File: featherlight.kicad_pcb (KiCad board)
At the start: 4 copper layers, 88.9 x 88.9 mm, 97 parts, among them IC1 BNO055, P1 USB_OTG, P10 CONN_01X06, P11 CONN_01X06, P12 CONN_01X06, P13 CONN_01X06, P14 CONN_01X06, P15 CONN_01X06, P16 CONN_01X06, P17 CONN_01X01, P18 CONN_01X01, P19 CONN_01X02, P2 CONN_01X06, P3 CONN_01X06, P4 CONN_01X06, P5 CONN_01X06, P6 CONN_01X06, P7 CONN_01X06, P8 CONN_01X06, P9 CONN_01X06, SW1 Button, SW2 Button, SW3 Button, SW4 Button, SW5 Button, U1 74AHCT1G125, U2 SAMD21G18, U3 AP2112, U4 MCP73831, Y1 32.768 KHz, Y2 32.768 KHz

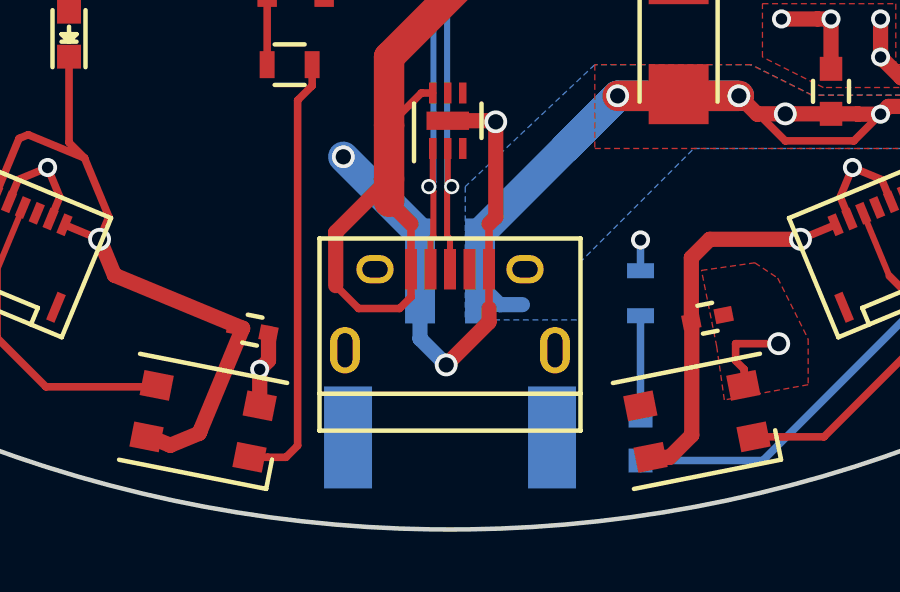
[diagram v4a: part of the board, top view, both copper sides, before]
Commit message: Changed PTH on the USB footprint to circular drills since Oshpark cannot into slots.
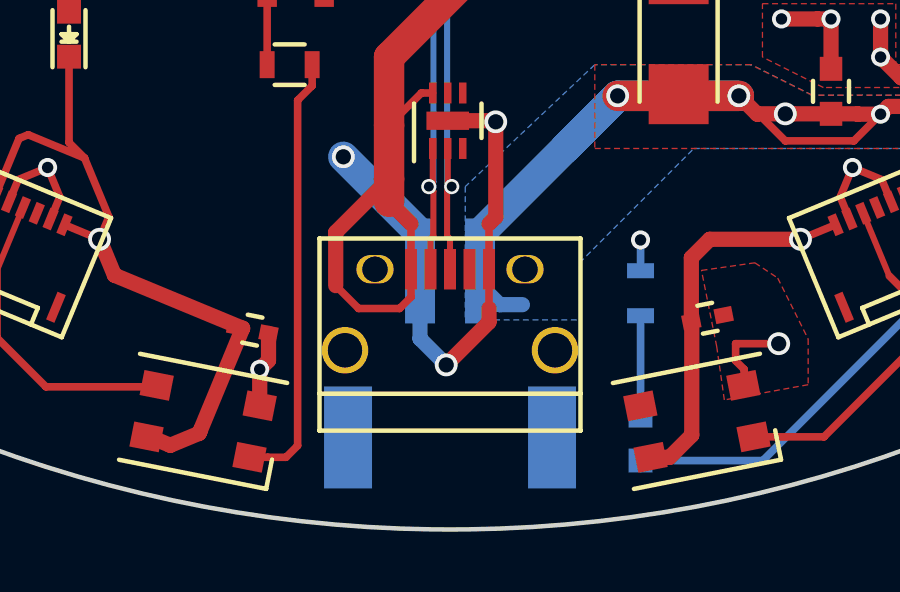
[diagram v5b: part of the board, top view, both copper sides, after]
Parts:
- P1: footprint Connect:USB_Micro-B -> featherlight:USB_Micro-B
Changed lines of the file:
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@@
-(kicad_pcb (version 20160815) (host pcbnew 4.1.0-alpha+201609050731+7118~50~ubuntu16.04.1-product)
+(kicad_pcb (version 20160815) (host pcbnew 4.1.0-alpha+201609080933+7135~55~ubuntu16.04.1-product)
   (general
     (links 297)
     (no_connects 3)
-    (area 57.074999 57.074999 146.125001 146.125001)
+    (area 54.872313 54.953833 148.378573 148.330281)
     (thickness 1.6002)
     (drawings 4)
@@
   )
   (setup
-    (last_trace_width 0.254)
+    (last_trace_width 0.2032)
     (user_trace_width 0.1524)
     (user_trace_width 0.2032)
@@
     )
   )
-  (module Connect:USB_Micro-B (layer F.Cu)
-    (at 101.6 138.938)
-    (descr "Micro USB Type B Receptacle")
-    (tags "USB USB_B USB_micro USB_OTG")
-    (attr smd)
-    (fp_text reference P1 (at 0 -3.45) (layer F.SilkS) hide
-      (effects (font (size 1 1) (thickness 0.15)))
-    )
-    (fp_text value USB_OTG (at 0 4.8) (layer F.Fab)
-      (effects (font (size 1 1) (thickness 0.15)))
-    )
-    (fp_line (start -4.6 -2.8) (end 4.6 -2.8) (layer F.CrtYd) (width 0.05))
-    (fp_line (start 4.6 -2.8) (end 4.6 4.05) (layer F.CrtYd) (width 0.05))
-    (fp_line (start 4.6 4.05) (end -4.6 4.05) (layer F.CrtYd) (width 0.05))
-    (fp_line (start -4.6 4.05) (end -4.6 -2.8) (layer F.CrtYd) (width 0.05))
-    (fp_line (start -4.3509 3.81746) (end 4.3491 3.81746) (layer F.SilkS) (width 0.15))
-    (fp_line (start -4.3509 -2.58754) (end 4.3491 -2.58754) (layer F.SilkS) (width 0.15))
-    (fp_line (start 4.3491 -2.58754) (end 4.3491 3.81746) (layer F.SilkS) (width 0.15))
-    (fp_line (start 4.3491 2.58746) (end -4.3509 2.58746) (layer F.SilkS) (width 0.15))
-    (fp_line (start -4.3509 3.81746) (end -4.3509 -2.58754) (layer F.SilkS) (width 0.15))
-    (pad 1 smd rect (at -1.3009 -1.56254 90) (size 1.35 0.4) (layers F.Cu F.Paste F.Mask)
-      (net 42 VUSB))
-    (pad 2 smd rect (at -0.6509 -1.56254 90) (size 1.35 0.4) (layers F.Cu F.Paste F.Mask)
-      (net 20 D-))
-    (pad 3 smd rect (at -0.0009 -1.56254 90) (size 1.35 0.4) (layers F.Cu F.Paste F.Mask)
-      (net 21 D+))
-    (pad 4 smd rect (at 0.6491 -1.56254 90) (size 1.35 0.4) (layers F.Cu F.Paste F.Mask))
-    (pad 5 smd rect (at 1.2991 -1.56254 90) (size 1.35 0.4) (layers F.Cu F.Paste F.Mask)
-      (net 1 GND))
-    (pad 6 thru_hole oval (at -2.5009 -1.56254 90) (size 0.95 1.25) (drill oval 0.55 0.85) (layers *.Cu *.Mask F.SilkS)
-      (net 28 "Net-(P1-Pad6)"))
-    (pad 6 thru_hole oval (at 2.4991 -1.56254 90) (size 0.95 1.25) (drill oval 0.55 0.85) (layers *.Cu *.Mask F.SilkS)
-      (net 28 "Net-(P1-Pad6)"))
-    (pad 6 thru_hole oval (at -3.5009 1.13746 90) (size 1.55 1) (drill oval 1.15 0.5) (layers *.Cu *.Mask F.SilkS)
-      (net 28 "Net-(P1-Pad6)"))
-    (pad 6 thru_hole oval (at 3.4991 1.13746 90) (size 1.55 1) (drill oval 1.15 0.5) (layers *.Cu *.Mask F.SilkS)
-      (net 28 "Net-(P1-Pad6)"))
-  )
   (module "Connector-FFC:Molex 503480-600" (layer F.Cu)
     (at 87.019761 136.79981 337.5)
@@
     )
   )
+  (module featherlight:USB_Micro-B (layer F.Cu)
+    (at 101.6 138.938)
+    (descr "Micro USB Type B Receptacle with circular plated through holes")
+    (tags "USB USB_B USB_micro USB_OTG")
+    (attr smd)
+    (fp_text reference P1 (at 0 -3.45) (layer F.SilkS) hide
+      (effects (font (size 1 1) (thickness 0.15)))
+    )
+    (fp_text value USB_OTG (at 0 4.8) (layer F.Fab)
+      (effects (font (size 1 1) (thickness 0.15)))
+    )
+    (fp_line (start -4.6 -2.8) (end 4.6 -2.8) (layer F.CrtYd) (width 0.05))
+    (fp_line (start 4.6 -2.8) (end 4.6 4.05) (layer F.CrtYd) (width 0.05))
+    (fp_line (start 4.6 4.05) (end -4.6 4.05) (layer F.CrtYd) (width 0.05))
+    (fp_line (start -4.6 4.05) (end -4.6 -2.8) (layer F.CrtYd) (width 0.05))
+    (fp_line (start -4.3509 3.81746) (end 4.3491 3.81746) (layer F.SilkS) (width 0.15))
+    (fp_line (start -4.3509 -2.58754) (end 4.3491 -2.58754) (layer F.SilkS) (width 0.15))
+    (fp_line (start 4.3491 -2.58754) (end 4.3491 3.81746) (layer F.SilkS) (width 0.15))
+    (fp_line (start 4.3491 2.58746) (end -4.3509 2.58746) (layer F.SilkS) (width 0.15))
+    (fp_line (start -4.3509 3.81746) (end -4.3509 -2.58754) (layer F.SilkS) (width 0.15))
+    (pad 1 smd rect (at -1.3009 -1.56254 90) (size 1.35 0.4) (layers F.Cu F.Paste F.Mask)
+      (net 42 VUSB))
+    (pad 2 smd rect (at -0.6509 -1.56254 90) (size 1.35 0.4) (layers F.Cu F.Paste F.Mask)
+      (net 20 D-))
+    (pad 3 smd rect (at -0.0009 -1.56254 90) (size 1.35 0.4) (layers F.Cu F.Paste F.Mask)
+      (net 21 D+))
+    (pad 4 smd rect (at 0.6491 -1.56254 90) (size 1.35 0.4) (layers F.Cu F.Paste F.Mask))
+    (pad 5 smd rect (at 1.2991 -1.56254 90) (size 1.35 0.4) (layers F.Cu F.Paste F.Mask)
+      (net 1 GND))
+    (pad 6 thru_hole oval (at -2.5009 -1.56254 90) (size 0.95 1.25) (drill 0.85) (layers *.Cu *.Mask F.SilkS)
+      (net 28 "Net-(P1-Pad6)"))
+    (pad 6 thru_hole oval (at 2.4991 -1.56254 90) (size 0.95 1.25) (drill 0.85) (layers *.Cu *.Mask F.SilkS)
+      (net 28 "Net-(P1-Pad6)"))
+    (pad 6 thru_hole circle (at -3.5009 1.13746 90) (size 1.55 1.55) (drill 1.15) (layers *.Cu *.Mask F.SilkS)
+      (net 28 "Net-(P1-Pad6)"))
+    (pad 6 thru_hole circle (at 3.4991 1.13746 90) (size 1.55 1.55) (drill 1.15) (layers *.Cu *.Mask F.SilkS)
+      (net 28 "Net-(P1-Pad6)"))
+  )
   (gr_text SWCLK (at 116.84 112.776) (layer B.SilkS)

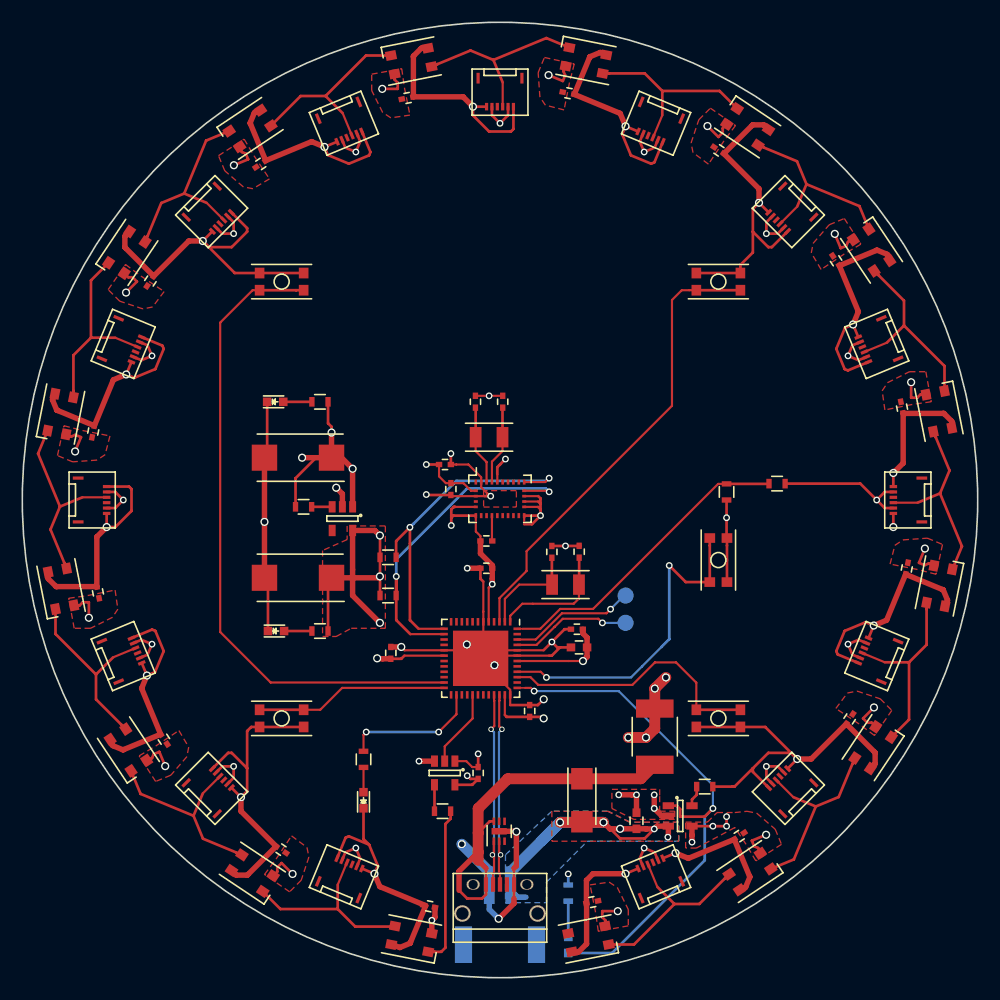
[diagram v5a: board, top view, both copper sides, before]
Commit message: Improper board size required full PCB redesign.
The rev A PCBs were far bigger than intended (target diameter was used as radius when laying it out).

Removed lipo circuit while reworking layout; will try to add it back in later.
Moved USB port to very edge of board to permit cable access.
Added +5V and ground contacts to ISP pads.
Swapped down to SAMD21E MCU for space reasons.
Removed connectors for space reasons.  Maybe they'll fit on the bottom?
Added fiducials front and back.
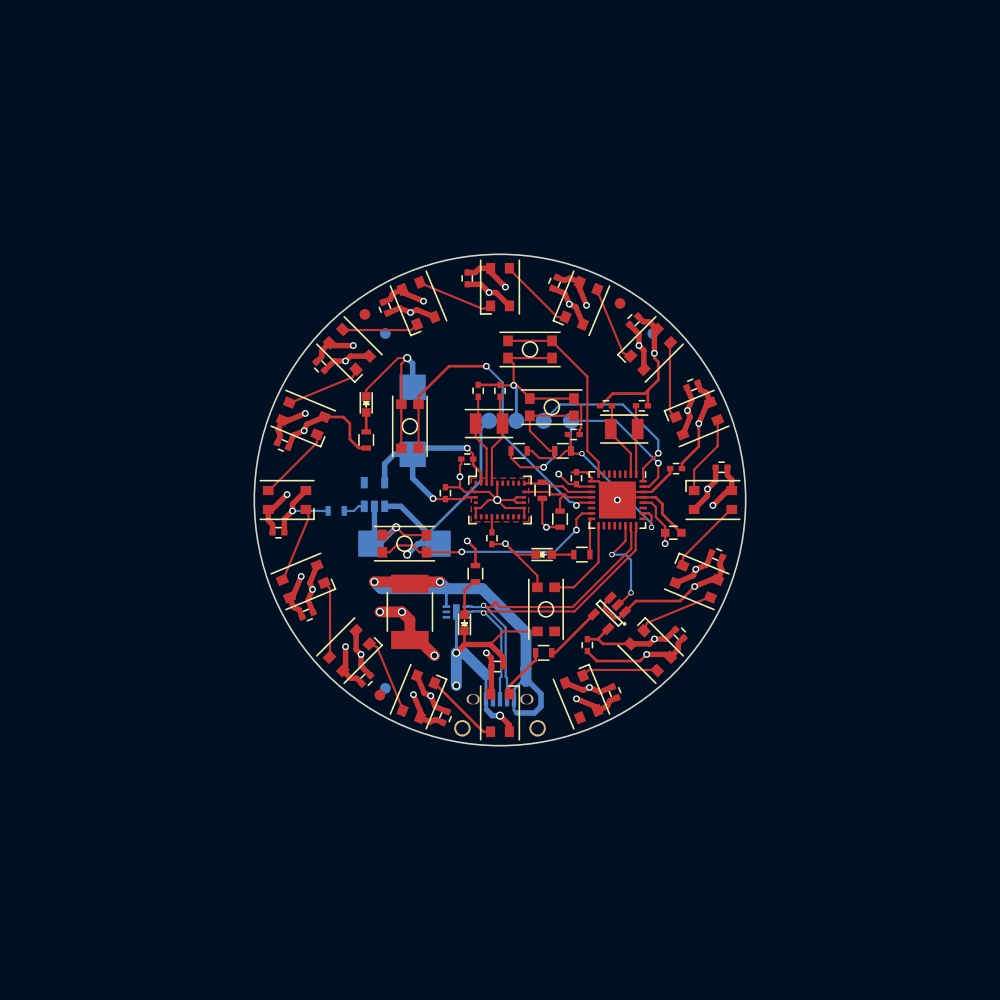
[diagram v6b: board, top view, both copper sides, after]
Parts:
- removed C20: 0.1 uF, Capacitors_SMD:C_0402
- removed C32: 4.7 uF, Capacitors_SMD:C_0603
- removed D21: D_Schottky, featherlight:DO-214AC
- removed D22: Green, LEDs:LED_0603
- removed P10, P11, P12, P13, P14, P15, P16, P2, P7, P8, P9: CONN_01X06, Connector-FFC:Molex 503480-600
- removed P17, P18: CONN_01X01, Measurement_Points:Measurement_Point_Round-SMD-Pad_Small
- removed P19: CONN_01X02, Connectors_JST:JST_PH_S2B-PH-SM4-TB_02x2.00mm_Angled
- removed R10: 10 K, Resistors_SMD:R_0603
- removed R11: 100 K, Resistors_SMD:R_0603
- removed U4: MCP73831, TO_SOT_Packages_SMD:SOT-23-5
- added FID1: Fiducial, Fiducials:Fiducial_1mm_Dia_2.54mm_Outer_CopperTop, F.Cu at (89.0, 84.3)
- added FID2: Fiducial, Fiducials:Fiducial_1mm_Dia_2.54mm_Outer_CopperTop, F.Cu at (112.8, 83.3)
- added FID3: Fiducial, Fiducials:Fiducial_1mm_Dia_2.54mm_Outer_CopperTop, F.Cu at (90.4, 119.8)
- added FID4: Fiducial, Fiducials:Fiducial_1mm_Dia_2.54mm_Outer_CopperTop, B.Cu at (90.9, 86.1)
- added FID5: Fiducial, Fiducials:Fiducial_1mm_Dia_2.54mm_Outer_CopperTop, B.Cu at (90.9, 119.1)
- added FID6: Fiducial, Fiducials:Fiducial_1mm_Dia_2.54mm_Outer_CopperTop, B.Cu at (115.8, 86.1)
- added R12: 1 K, Resistors_SMD:R_0603, B.Cu at (107.4, 97.0)
- C17, C18, D17, P1, R2, U3: moved to B.Cu
- P3, P4, P5, P6: value CONN_01X06 -> CONN_01X01; footprint Connector-FFC:Molex 503480-600 -> Measurement_Points:Measurement_Point_Round-SMD-Pad_Small; moved to B.Cu
- R5: value 100 K -> 10 K
- R9: moved to F.Cu
- U2: value SAMD21G18 -> SAMD21E18A-M; footprint Housings_DFN_QFN:QFN-48-1EP_7x7mm_Pitch0.5mm -> Housings_DFN_QFN:QFN-32-1EP_5x5mm_Pitch0.5mm
- moved P3 48.0 mm to (108.2, 94.2), turned to 0 degrees
- moved P4 45.0 mm to (105.7, 94.2), turned to 0 degrees
- moved R9 41.2 mm to (107.4, 97.0), turned to 180 degrees
- moved P5 37.8 mm to (100.6, 94.2), turned to 0 degrees
- moved P6 37.4 mm to (103.1, 94.2), turned to 0 degrees
- moved D18 28.3 mm to (105.7, 106.7), turned to 0 degrees
- moved R6 27.9 mm to (109.2, 106.7), turned to 0 degrees
- moved C19 26.5 mm to (108.5, 95.5), turned to 180 degrees
- moved F1 25.6 mm to (93.2, 112.0), turned to 270 degrees
- moved R5 24.2 mm to (103.4, 97.0)
- moved C1 23.2 mm to (101.3, 117.1), turned to 0 degrees
- moved D1 22.6 mm to (101.6, 121.4), turned to 90 degrees
- moved D16 22.6 mm to (109.2, 119.9), turned to 112.5 degrees
- moved D10 22.5 mm to (109.2, 83.3), turned to 247.5 degrees
- moved D14 22.5 mm to (119.9, 109.2), turned to 157.5 degrees
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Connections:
- C19 pad 1: +3V3 -> GND
- C19 pad 2: GND -> /MCU + IMU/~RST~
- P3 pad 1: GND -> SWCLK
- P4 pad 1: GND -> SWDIO
- P5 pad 1: GND -> VDD
- R5 pad 1: VDD_MON -> +3V3
- R5 pad 2: VDD -> /MCU + IMU/~RST~
- R9 pad 1: VDD -> /MCU + IMU/~RST~
- R9 pad 2: Net-(D22-Pad2) -> Net-(R9-Pad2)
- SW1 pad 2: /MCU + IMU/~RST~ -> Net-(R9-Pad2)
- U2 pad 10: (no net) -> GND
- U2 pad 11: (no net) -> /MCU + IMU/SDA
- U2 pad 12: (no net) -> /MCU + IMU/SCL
- U2 pad 13: /MCU + IMU/SDA -> /MCU + IMU/UL_BUTTON
- U2 pad 14: /MCU + IMU/SCL -> (no net)
- U2 pad 15: (no net) -> /MCU + IMU/LL_BUTTON
- U2 pad 16: (no net) -> Net-(R6-Pad2)
- U2 pad 17: +3V3 -> /MCU + IMU/LR_BUTTON
- U2 pad 18: GND -> (no net)
- U2 pad 22: (no net) -> Net-(U1-Pad2)
- U2 pad 23: /MCU + IMU/UL_BUTTON -> D-
- U2 pad 24: /MCU + IMU/LL_BUTTON -> D+
- U2 pad 26: Net-(R6-Pad2) -> /MCU + IMU/~RST~
- U2 pad 28: (no net) -> GND
- U2 pad 29: Net-(U1-Pad2) -> +3V3
- U2 pad 3: /MCU + IMU/UR_BUTTON -> (no net)
- U2 pad 30: (no net) -> +3V3
- U2 pad 31: (no net) -> SWCLK
- U2 pad 32: (no net) -> SWDIO
- U2 pad 33: D- -> +3V3
- U2 pad 5: GND -> (no net)
- U2 pad 6: +3V3 -> (no net)
- U2 pad 8: (no net) -> /MCU + IMU/UR_BUTTON
- U2 pad 9: (no net) -> +3V3
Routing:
- net GND: track 470.2 -> 223.0 mm, vias 39 -> 26
- net CHARGE_STATUS: track 50.8 -> 0.00 mm, vias 2 -> 0
- net +3V3: track 106.6 -> 61.9 mm, vias 12 -> 6
- net +BATT: track 33.7 -> 0.00 mm, vias 5 -> 0
- net /MCU + IMU/UL_BUTTON: track 60.6 -> 30.4 mm, vias 0 -> 2
- net VDD_MON: track 29.0 -> 0.00 mm
- net VDD: track 150.7 -> 123.3 mm, vias 44 -> 20
- net /MCU + IMU/SDA: track 33.0 -> 6.61 mm, vias 2 -> 0
- net /MCU + IMU/UR_BUTTON: track 43.3 -> 18.3 mm
- net /MCU + IMU/SCL: track 31.9 -> 8.20 mm, vias 2 -> 0
- net SWDIO: track 0.00 -> 17.1 mm, vias 0 -> 1
- net /MCU + IMU/LR_BUTTON: track 25.2 -> 8.46 mm
- net SWCLK: track 0.00 -> 15.6 mm, vias 0 -> 1
- net /MCU + IMU/~RST~: track 31.2 -> 18.9 mm
- net /MCU + IMU/SWDIO: track 11.8 -> 0.00 mm, vias 1 -> 0
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- removed copper zone on F.Cu, net +3V3
- removed copper zone on B.Cu, net +BATT
- removed copper zone on F.Cu, net +BATT
- removed copper zone on F.Cu, net VDD
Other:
- board size 88.9 x 88.9 mm -> 45.7 x 45.7 mm
- net class Default: clearance 0.2032 -> 0.127
- net class Power: clearance 0.2032 -> 0.127
- rule trace_clearance: 0.2032 -> 0.127
- rule trace_min: 0.1524 -> 0.127
- rule via_min_drill: 0.3302 -> 0.254
- rule via_min_size: 0.508 -> 0.3556
- board text added: "+5"
- board text added: "Featherlight Rev B"
- board text added: "GND"
- board text removed: "Featherlight Prototype Rev B"

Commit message: Re-added lipo circuit.
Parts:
- added C20: 4.7 uF, Capacitors_SMD:C_0603, B.Cu at (106.4, 107.7)
- added D21: Green, LEDs:LED_0603, F.Cu at (106.4, 121.2)
- added D22: D_Schottky, featherlight:DO-214AC, F.Cu at (91.7, 100.8)
- added P2: CONN_01X02, Connectors_JST:JST_PH_S2B-PH-SM4-TB_02x2.00mm_Angled, B.Cu at (114.3, 114.0)
- added R10: 100 K, Resistors_SMD:R_0603, B.Cu at (111.0, 88.2)
- added R11: 470, Resistors_SMD:R_0603, B.Cu at (109.7, 121.4)
- added R13: 100 K, Resistors_SMD:R_0603, F.Cu at (111.0, 88.2)
- added R14: 10 K, Resistors_SMD:R_0603, B.Cu at (102.9, 108.7)
- added U4: MCP73831, TO_SOT_Packages_SMD:SOT-23-5, B.Cu at (105.9, 110.7)
- moved C24 0.78 mm to (112.0, 92.3), turned to 270 degrees
- renumbered D20 to D19, D19 to D20, R7 to R2, R8 to R7, R2 to R8
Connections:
- U2 pad 19: (no net) -> CHARGE_STATUS
- U2 pad 6: (no net) -> VDD_MON
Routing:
- net +BATT: track 0.00 -> 30.0 mm, vias 0 -> 2
- net CHARGE_STATUS: track 0.00 -> 28.5 mm, vias 0 -> 2
- net GND: track 223.0 -> 243.3 mm, vias 26 -> 27
- net VDD: track 123.3 -> 139.3 mm
- net VDD_MON: track 0.00 -> 12.2 mm, vias 0 -> 1
- net VUSB: track 38.7 -> 50.7 mm
- net Net-(R14-Pad1): track 0.00 -> 4.42 mm
- net Net-(D21-Pad2): track 0.00 -> 3.64 mm, vias 0 -> 1
- net /MCU + IMU/LL_BUTTON: track 22.1 -> 22.8 mm
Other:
- net class Default: clearance 0.127 -> 0.2032
- net class Power: clearance 0.127 -> 0.2032
- rule trace_clearance: 0.127 -> 0.2032
